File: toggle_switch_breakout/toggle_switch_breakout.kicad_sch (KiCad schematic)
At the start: 3 parts, among them J1 Conn_01x04_Pin, SW1 SW_SPST, SW2 SW_SPST

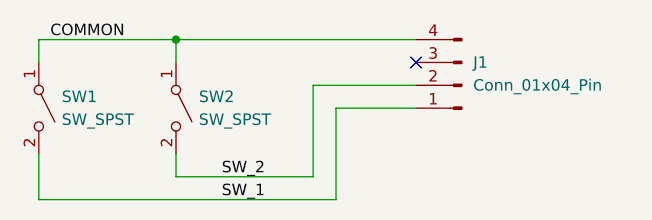
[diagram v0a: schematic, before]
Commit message: Added casing cad files
Designed a case in Onshape, made minor revisions to breakout boards.
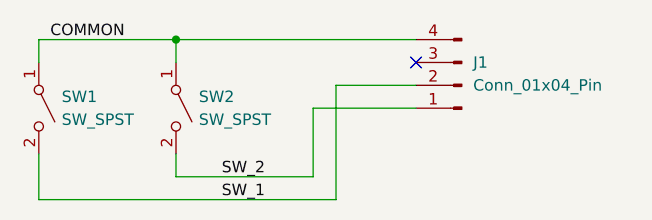
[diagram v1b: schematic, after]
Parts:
- J1: footprint Connector_PinHeader_2.54mm:PinHeader_1x04_P2.54mm_Horizontal -> Connector_PinHeader_2.54mm:PinHeader_1x04_P2.54mm_Vertical
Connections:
- net SW_1: now also J1.2 (Pin_2); no longer J1.1 (Pin_1)
- net SW_2: now also J1.1 (Pin_1); no longer J1.2 (Pin_2)
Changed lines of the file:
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@@
 	(title_block
 		(title "Toggle Switch Breakout Schematic")
-		(date "2024-06-07")
-		(rev "0.1.0")
+		(date "2024-06-08")
+		(rev "0.1.1")
 	)
 	(junction
@@
 	(wire
 		(pts
-			(xy 121.92 78.74) (xy 121.92 68.58)
+			(xy 121.92 66.04) (xy 130.81 66.04)
+		)
+		(stroke
+			(width 0)
+			(type default)
+		)
+	)
+	(wire
+		(pts
+			(xy 119.38 68.58) (xy 119.38 76.2)
+		)
+		(stroke
+			(width 0)
+			(type default)
+		)
+	)
+	(wire
+		(pts
+			(xy 121.92 66.04) (xy 121.92 78.74)
 		)
 		(stroke
@@
 	(wire
 		(pts
-			(xy 121.92 68.58) (xy 130.81 68.58)
+			(xy 119.38 68.58) (xy 130.81 68.58)
 		)
 		(stroke
@@
 		(pts
 			(xy 88.9 60.96) (xy 104.14 60.96)
-		)
-		(stroke
-			(width 0)
-			(type default)
-		)
-	)
-	(wire
-		(pts
-			(xy 119.38 66.04) (xy 119.38 76.2)
 		)
 		(stroke
@@
 		(pts
 			(xy 88.9 60.96) (xy 88.9 63.5)
-		)
-		(stroke
-			(width 0)
-			(type default)
-		)
-	)
-	(wire
-		(pts
-			(xy 119.38 66.04) (xy 130.81 66.04)
 		)
 		(stroke
@@
 			)
 		)
-		(property "Footprint" "Connector_PinHeader_2.54mm:PinHeader_1x04_P2.54mm_Horizontal"
+		(property "Footprint" "Connector_PinHeader_2.54mm:PinHeader_1x04_P2.54mm_Vertical"
 			(at 135.89 66.04 0)
 			(effects
